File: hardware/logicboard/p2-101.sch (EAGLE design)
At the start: 67 parts, among them IC1 74LS06N, IC11 74LS153D, IC12 LTC485S, IC13 LTC485S, IC2 4066N, J1 MKR, J11 Qwiic, J12 Qwiic, J13 Qwiic, J14 Qwiic, J2 GPIO, J3 Vcc, J4 RLY, J5 SPI, J6 LED, K1 G5V1, T1 2SC1815, U1 DS18B20

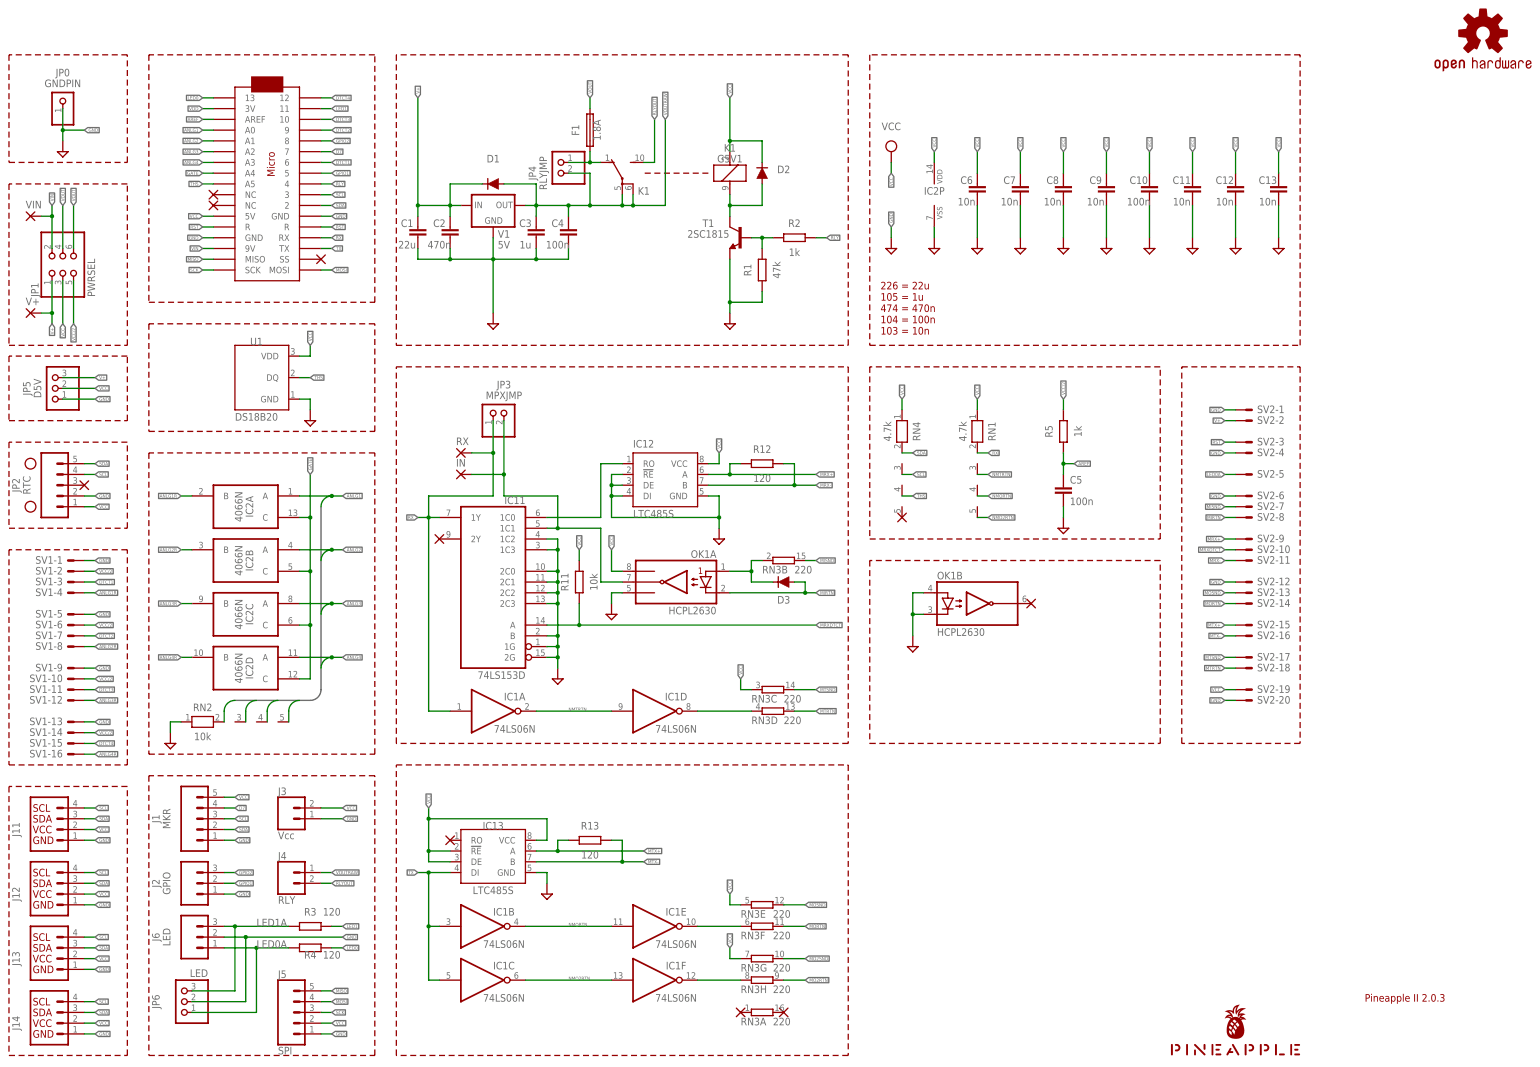
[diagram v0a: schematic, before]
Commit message: Removed Arduino.
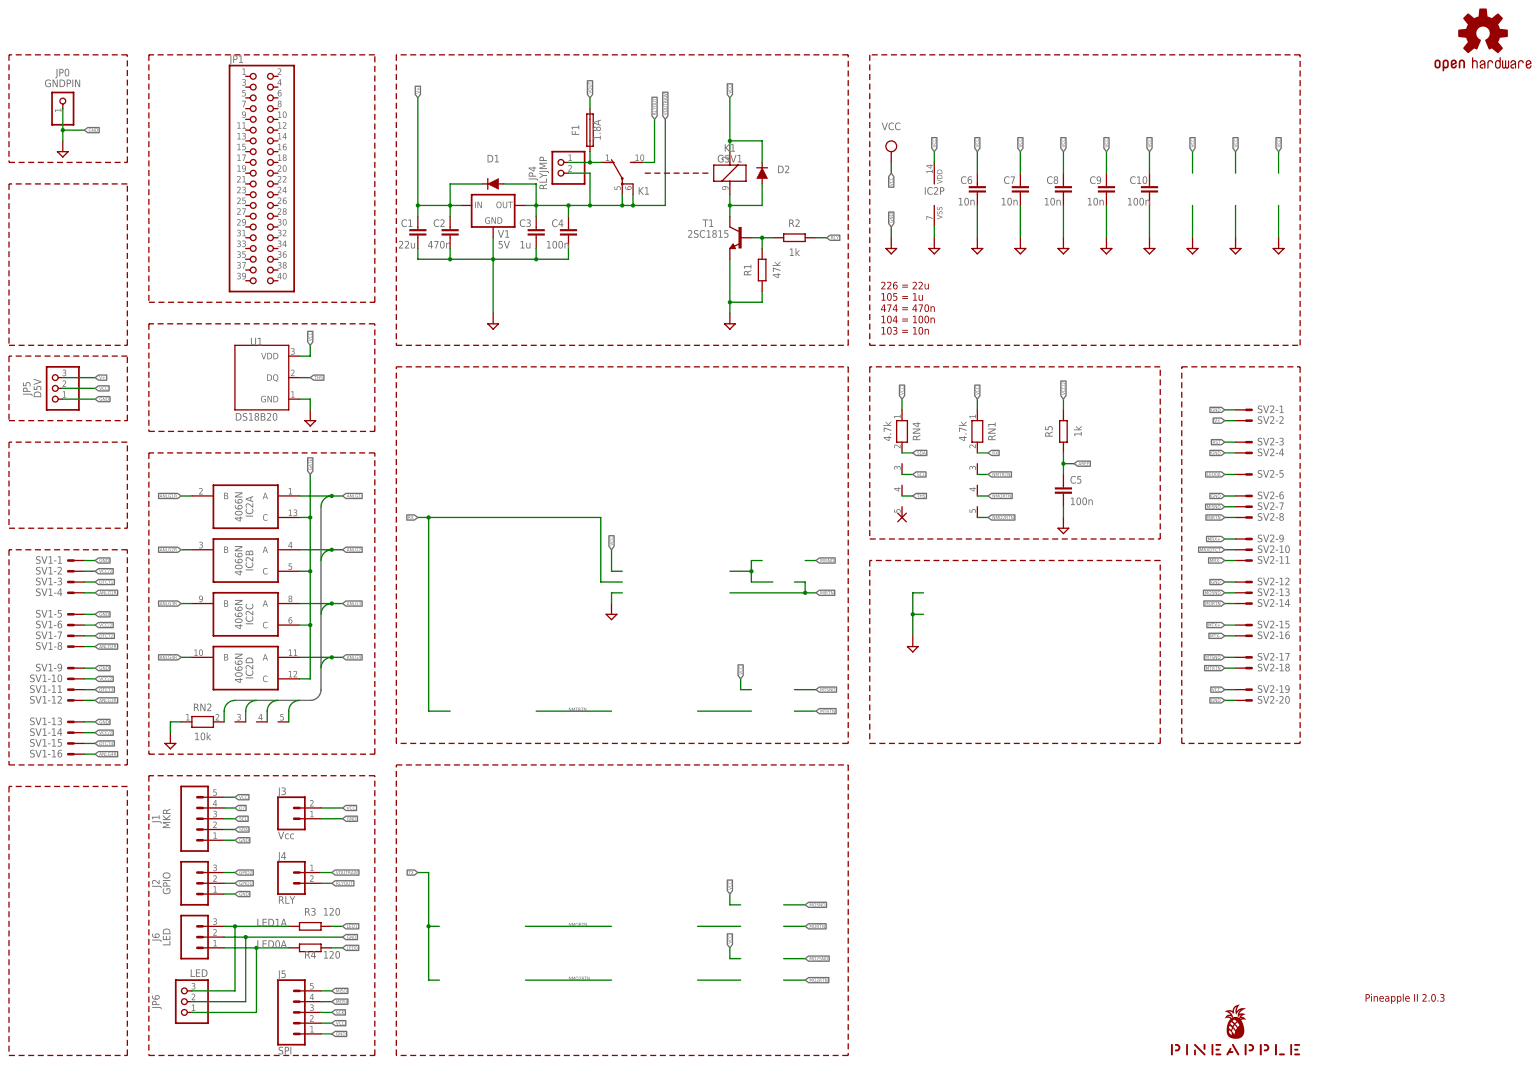
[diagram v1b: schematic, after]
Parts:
- removed C11, C12, C13: 10n, rcl:C-EUC2012
- removed D3: DIODE-1N4148, SparkFun-DiscreteSemi:DIODE-1N4148
- removed H1, H2: STAND-OFF, SparkFun-Hardware:STAND-OFF
- removed IC1: 74LS06N, 74xx-us:74LS06N
- removed IC11: 74LS153D, 74xx-us:74LS153D
- removed IC12, IC13: LTC485S, linear-technology:LTC485S
- removed IN, RX, V+, VIN: (no value), wirepad:SMD2
- removed J11, J12, J13, J14: Qwiic, SparkFun-Connectors:QWIIC_CONNECTORJS-1MM
- removed JP2: RTC, SparkFun-Connectors:CONN_05
- removed JP3: MPXJMP, pinhead:PINHD-1X2
- removed MC1: ARDUINOMICRO, adafruit:ARDUINOMICRO
- removed OK1: HCPL2630, optocoupler:HCPL2630
- removed R11: 10k, rcl:R-EU_M2012
- removed R12, R13: 120, rcl:R-EU_M2012
- removed RN3: 220, resistor-dil:8R-N
- JP1: value PWRSEL -> (none); device pinhead:PINHD-2X3 -> pinhead:PINHD-2X20
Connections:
- removed net MIDIINSND: D3.C, OK1A.A1, RN3B.1
- removed net MIN: IC11A.1C1, IN.P, JP3.2, OK1A.VO1
- removed net MO2RTN: RN3H.2
- removed net MO2RTNRAW: IC1F.O, RN3H.1
- removed net MO2SND: RN3G.2
- removed net MORTNRAW: IC1E.O, RN3F.1
- removed net MRX: IC11A.1C0, IC12.RO
- removed net MTRTNRAW: IC1D.O, RN3D.1
- removed net TX: IC13.DI, IC1B.I, IC1C.I, MC1.TX
- removed net VDD: MC1.3V
- removed net VIN: JP1.2, MC1.9V, VIN.P
- net ANLG1: no longer MC1.A0
- net ANLG2: no longer MC1.A1
- net ANLG3: no longer MC1.A2
- net ANLG4: no longer MC1.A3
- net AREF: no longer MC1.AREF
- net D7: no longer MC1.7
- net DTCT1: no longer MC1.6
- net DTCT2: no longer MC1.9
- net DTCT3: no longer MC1.10
- net DTCT4: no longer MC1.12
- net GATE: no longer MC1.A4
- net GND: no longer C11.2, C12.2, C13.2, IC11A.1C2, IC11A.1C3, IC11A.1G, IC11A.2C0, IC11A.2C1, IC11A.2C2, IC11A.2C3, IC11A.2G, IC11A.B, IC12.!RE, IC12.DE, IC12.DI, IC12.GND, IC13.GND, J11.GND, J12.GND, J13.GND, J14.GND, JP2.2, MC1.GND, MC1.GND@1, OK1A.GND, OK1B.A2, OK1B.C2
- net GPIO1: no longer MC1.5
- net GPIO2: no longer MC1.8
- net LED0: no longer MC1.13
- net LED1: no longer MC1.11
- net MIRTN: no longer D3.A, OK1A.C1
- net MISND: no longer RN3B.2
- net MISO: no longer MC1.MISO
- net MORTN: no longer RN3F.2
- net MOSI: no longer MC1.MOSI
- net MOSND: no longer RN3E.2
- net MRX+: no longer IC12.A, R12.1
- net MRX-: no longer IC12.B, R12.2
- net MRXDTCT: no longer IC11A.A, R11.1
- net MTRTN: no longer RN3D.2
- net MTSND: no longer RN3C.2
- net MTX+: no longer IC13.A, R13.1
- net MTX-: no longer IC13.B, R13.2
- net NMO2RTN: no longer IC1C.O, IC1F.I
- net NMORTN: no longer IC1B.O, IC1E.I
- net NMTRTN: no longer IC1A.O, IC1D.I
- net RLY: no longer MC1.4
- net RST: no longer MC1.R@1, MC1.R@2
- net RX: no longer IC11A.1Y, IC1A.I, JP3.1, MC1.RX, RX.P
- net SCK: no longer MC1.SCK
- net SCL: no longer J11.SCL, J12.SCL, J13.SCL, J14.SCL, JP2.4, MC1.3
- net SDA: no longer J11.SDA, J12.SDA, J13.SDA, J14.SDA, JP2.5, MC1.2
- net THS: no longer MC1.A5
- net V+: no longer JP1.1, V+.P
- net VCC: no longer C11.1, C12.1, C13.1, IC12.VCC, IC13.!RE, IC13.DE, IC13.VCC, J11.VCC, J12.VCC, J13.VCC, J14.VCC, JP1.3, JP2.1, MC1.5V, OK1A.VCC, R11.2, RN3C.1, RN3E.1, RN3G.1
- net VCC/2: no longer JP1.5
- net VOUT: no longer JP1.4, JP1.6

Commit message: Unknown...
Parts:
- removed C10, C4, C5: 100n, rcl:C-EU025-024X044
- removed C3: 1u, rcl:C-EU050-024X044
- removed C6, C7, C8, C9: 10n, resistor:C-EU025-024X044
- removed D1, D2: DIODE-1N4148, SparkFun-DiscreteSemi:DIODE-1N4148
- removed F1: 1.8A, fuse:TE5
- removed J4: RLY, SparkFun-Connectors:CONN_02-JST-2MM-SMT
- removed J6: LED, SparkFun-Connectors:CONN_03JST-PTH
- removed JP0: GNDPIN, pinhead:PINHD-1X1
- removed JP4: RLYJMP, pinhead:PINHD-1X2
- removed JP5: D5V, pinhead:PINHD-1X3
- removed JP6: LED, pinhead:PINHD-1X3
- removed K1: G5V1, relay:G5V1
- removed RN1, RN4: 4.7k, resistor-net:RN04
- removed RN2: 10k, resistor-net:RN04
- removed SV2: (no value), con-ml:ML20LE
- removed T1: 2SC1815, transistor:2SC1815
- removed V1: 5V, v-reg:78XXL
- added R6, R7, R8: (no value), rcl:R-EU_M2012
- C1: value 22u -> (none); device rcl:C-EU025-050X050 -> rcl:C-EUC2012
- C2: value 470n -> (none); device rcl:C-EU050-024X044 -> rcl:C-EUC2012
- IC2: value 4066N -> 4066D; device 40xx:4066N -> 40xx:4066D
- R1: value 47k -> (none); device resistor:R-EU_0204/5 -> rcl:R-EU_M2012
- R2, R5: value 1k -> (none); device resistor:R-EU_0204/5 -> rcl:R-EU_M2012
- R3, R4: value 120 -> (none); device resistor:R-EU_0204/5 -> rcl:R-EU_M2012
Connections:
- removed net LED0: R4.2
- removed net LED0A: J6.1, JP6.1, R4.1, SV2-5.S
- removed net LED1: R3.2
- removed net LED1A: J6.3, JP6.3, R3.1
- removed net MIRTN: SV2-8.S
- removed net MISND: SV2-7.S
- removed net MORTN: SV2-14.S
- removed net MOSND: SV2-13.S
- removed net MRX+: SV2-9.S
- removed net MRX-: SV2-11.S
- removed net MRXDTCT: SV2-10.S
- removed net MTRTN: SV2-18.S
- removed net MTSND: SV2-17.S
- removed net MTX+: SV2-15.S
- removed net MTX-: SV2-16.S
- removed net NMO2RTN: RN1.5
- removed net NMORTN: RN1.4
- removed net NMTRTN: RN1.3
- removed net RLY: R2.2
- removed net RLYDRV: R1.2, R2.1, T1.B
- removed net RLYOUT: J4.1, K12.S
- removed net RLYSNK: D2.A, K11.2, T1.C
- removed net RST: SV2-3.S
- removed net V+: C1.1, C2.1, D1.C, JP5.3, SV2-2.S, V1.IN
- removed net VOUT: F1.2
- removed net VOUTRAW: C3.1, C4.1, D1.A, J4.2, JP4.2, K12.P, K12.P@1, V1.OUT
- removed net VOUTRAW2: F1.1, JP4.1, K12.O
- new net CE0: JP1.24
- new net CE1: JP1.26
- new net EEPROMSCL: JP1.28
- new net EEPROMSDA: JP1.27
- new net GPCLK0: JP1.7
- new net GPIO16: JP1.36
- new net GPIO17: JP1.11
- new net GPIO22: JP1.15
- new net GPIO23: JP1.16
- new net GPIO24: JP1.18
- new net GPIO25: JP1.22
- new net GPIO26: JP1.37
- new net GPIO27: JP1.13
- new net GPIO5: JP1.29
- new net GPIO6: JP1.31
- new net MISO0: JP1.21
- new net MOSI0: JP1.19
- new net PCMCLK: JP1.12
- new net PCMDIN: JP1.38
- new net PCMDOUT: JP1.40
- new net PCMFS: JP1.35
- new net PWM0: JP1.32
- new net PWM1: JP1.33
- new net SCL1: JP1.5
- new net SCLK0: JP1.23
- new net SDA1: JP1.3
- new net TX: JP1.8
- new net VDD: JP1.1, JP1.17
- net ANLG1: now also R1.2; no longer RN2.2
- net ANLG2: now also R2.2; no longer RN2.3
- net ANLG3: now also R3.2; no longer RN2.4
- net ANLG4: now also R4.2; no longer RN2.5
- net AREF: now also C2.1, R8.2; no longer C5.1, R5.1
- net GND: now also JP1.14, JP1.20, JP1.25, JP1.30, JP1.34, JP1.39, JP1.6, JP1.9, R2.1, R3.1, R4.1; no longer C10.2, C3.2, C4.2, C5.2, C6.2, C7.2, C8.2, C9.2, J6.2, JP0.1, JP5.1, JP6.2, RN2.1, SV2-1.S, SV2-12.S, SV2-20.S, SV2-4.S, SV2-6.S, T1.E, V1.GND
- net RX: now also JP1.10; no longer RN1.2
- net SCL: now also R6.2; no longer RN4.3
- net SDA: now also R5.2; no longer RN4.2
- net THS: now also R7.2; no longer RN4.4
- net VCC: now also C1.1, JP1.2, JP1.4, R5.1, R6.1, R7.1, R8.1; no longer C10.1, C6.1, C7.1, C8.1, C9.1, D2.C, JP5.2, K11.1, RN1.1, RN4.1, SV2-19.S
- net VCC/2: no longer R5.2
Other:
- moved on the sheet: C1, C2, R1, R2, R3, R4, R5
